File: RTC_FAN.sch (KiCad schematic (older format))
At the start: 9 parts

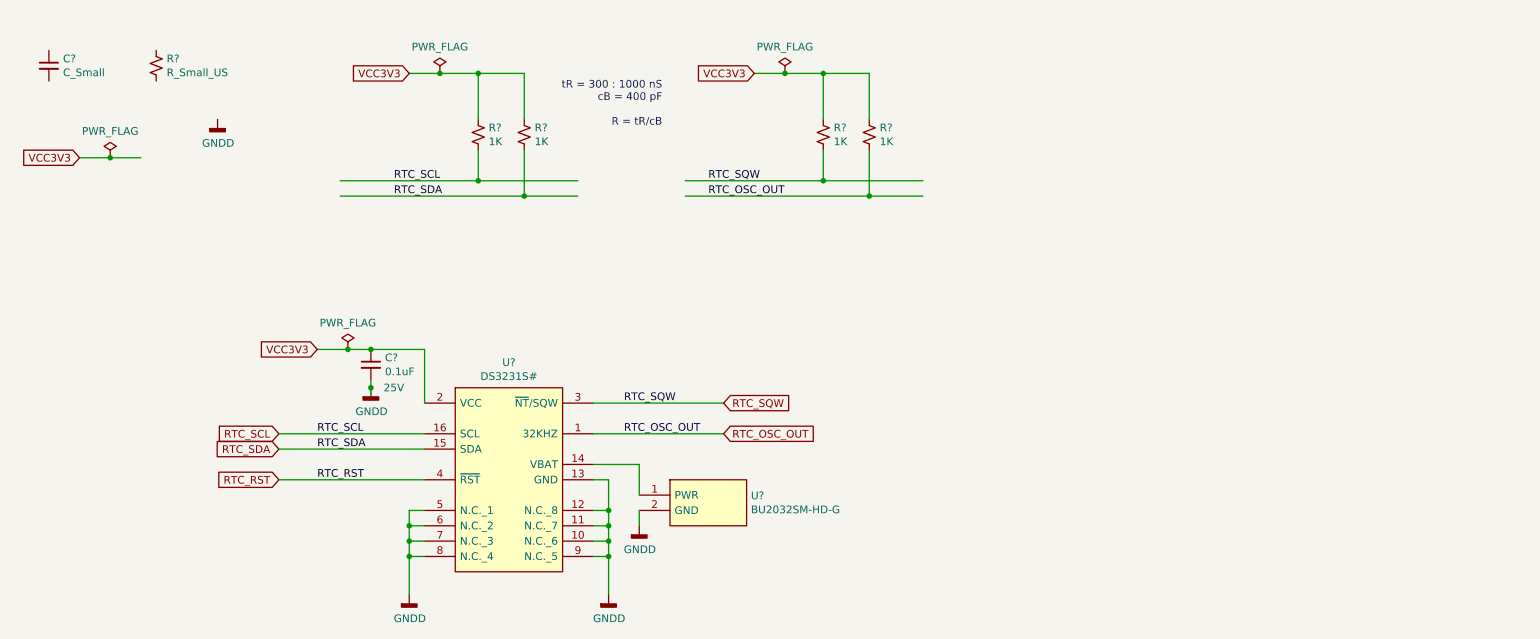
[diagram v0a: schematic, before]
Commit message: Added fan control circuitry
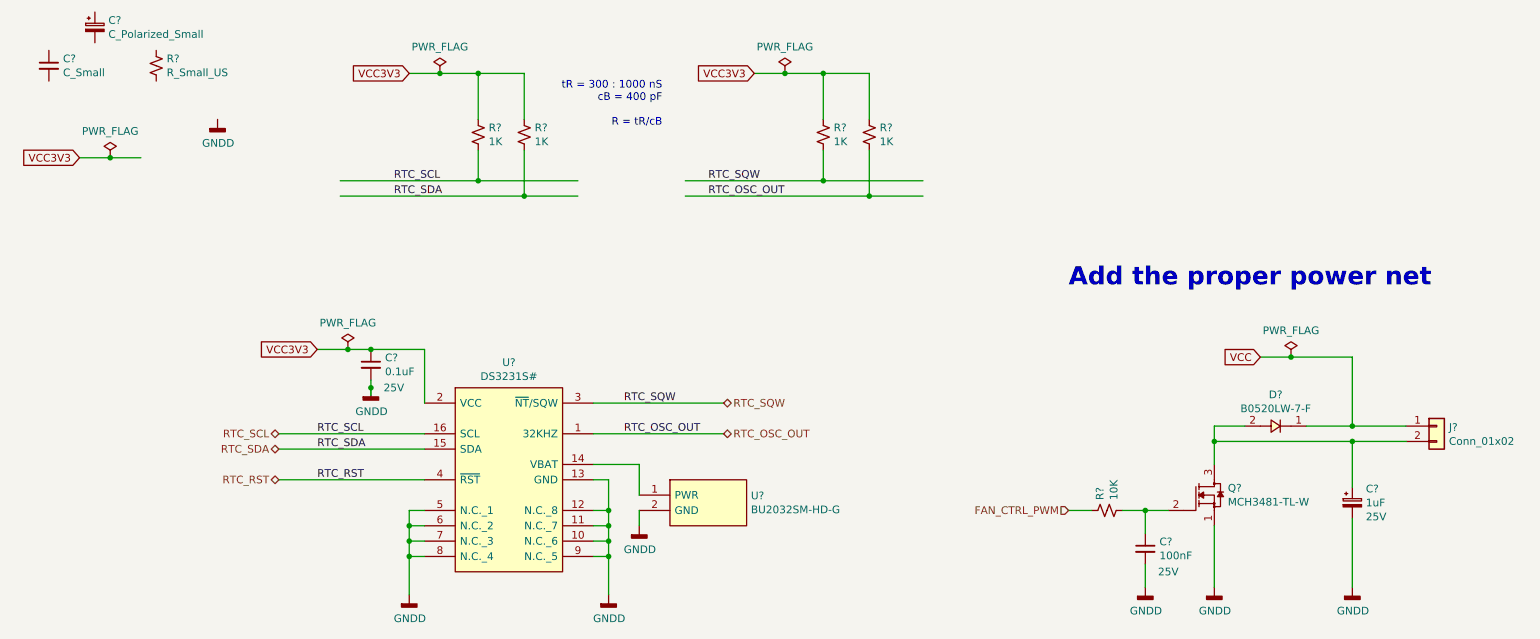
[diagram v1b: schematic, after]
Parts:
- added C?: 100nF, Capacitor_SMD:C_0603_1608Metric_Pad1.08x0.95mm_HandSolder, symbol Device:C_Small
- added C?: C_Polarized_Small, Capacitor_Tantalum_SMD:CP_EIA-1608-10_AVX-L_Pad1.25x1.05mm_HandSolder, symbol Device:C_Polarized_Small
- added C?: 1uF, Capacitor_Tantalum_SMD:CP_EIA-1608-10_AVX-L_Pad1.25x1.05mm_HandSolder, symbol Device:C_Polarized_Small
- added D?: B0520LW-7-F, SOD3716X145N, symbol GM_Diodes:B0520LW-7-F
- added J?: Conn_01x02, Connector_PinHeader_1.27mm:PinHeader_1x02_P1.27mm_Vertical, symbol Connector_Generic:Conn_01x02
- added Q?: MCH3481-TL-W, GM_SOT:SOT65P270X085-3N, symbol GM_MOSFET:MCH3481-TL-W
- added R?: 10K, Resistor_SMD:R_0603_1608Metric_Pad0.98x0.95mm_HandSolder, symbol Device:R_Small_US
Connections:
- net labels added: FAN_CTRL_PWM, VCC
- wire segments 56 -> 74
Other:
- note added: "Add the proper power net"
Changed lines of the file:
@@
 Text Label 4500 3300 0    50   ~ 0
-RTC_OSC_OUT
-Text GLabel 2250 3300 0    50   Input ~ 0
-RTC_SCL
-Text GLabel 2250 3400 0    50   Input ~ 0
-RTC_SDA
-Text GLabel 2250 3600 0    50   Input ~ 0
-RTC_RST
-Text GLabel 5150 3100 2    50   Input ~ 0
-RTC_SQW
-Text GLabel 5150 3300 2    50   Input ~ 0
 RTC_OSC_OUT
 Wire Wire Line
@@
 Wire Wire Line
 	4600 3500 4300 3500
+$Comp
+L GM_MOSFET:MCH3481-TL-W Q?
+U 1 1 602539F0
+P 8250 3700
+F 0 "Q?" H 8438 3746 50  0000 L CNN
+F 1 "MCH3481-TL-W" H 8438 3655 50  0000 L CNN
+F 2 "GM_SOT:SOT65P270X085-3N" H 9250 3900 50  0001 C CNN
+F 3 "https://www.onsemi.com/pub/Collateral/MCH3481-D.PDF" H 8250 4000 50  0001 C CNN
+F 4 "MCH3481-TL-W" H 9050 4000 50  0001 C CNN "MPN"
+	1    8250 3700
+	1    0    0    -1
+$EndComp
+$Comp
+L Device:R_Small_US R?
+U 1 1 60254F0F
+P 7650 3800
+AR Path="/601E7C5A/60254F0F" Ref="R?"  Part="1"
+AR Path="/601E7CC8/60254F0F" Ref="R?"  Part="1"
+F 0 "R?" H 7718 3846 50  0000 L CNN
+F 1 "10K" H 7718 3755 50  0000 L CNN
+F 2 "Resistor_SMD:R_0603_1608Metric_Pad0.98x0.95mm_HandSolder" H 7650 3800 50  0001 C CNN
+F 3 "~" H 7650 3800 50  0001 C CNN
+	1    7650 3800
+	0    -1   -1   0
+$EndComp
+$Comp
+L Device:C_Small C?
+U 1 1 60254F16
+P 7900 4050
+AR Path="/601E7C5A/60254F16" Ref="C?"  Part="1"
+AR Path="/601E7CC8/60254F16" Ref="C?"  Part="1"
+F 0 "C?" H 7992 4096 50  0000 L CNN
+F 1 "100nF" H 7992 4005 50  0000 L CNN
+F 2 "Capacitor_SMD:C_0603_1608Metric_Pad1.08x0.95mm_HandSolder" H 7900 4050 50  0001 C CNN
+F 3 "~" H 7900 4050 50  0001 C CNN
+F 4 "25V" H 8050 3900 50  0000 C CNN "Voltage"
+	1    7900 4050
+	1    0    0    -1
+$EndComp
+Wire Wire Line
+	7750 3800 7900 3800
+Wire Wire Line
+	7900 3950 7900 3800
+Connection ~ 7900 3800
+Wire Wire Line
+	7900 3800 8050 3800
+$Comp
+L power:GNDD #PWR?
+U 1 1 6025D5E9
+P 7900 4300
+AR Path="/601DF0A6/6025D5E9" Ref="#PWR?"  Part="1"
+AR Path="/601E7C5A/6025D5E9" Ref="#PWR?"  Part="1"
+AR Path="/601E7CC8/6025D5E9" Ref="#PWR?"  Part="1"
+F 0 "#PWR?" H 7900 4050 50  0001 C CNN
+F 1 "GNDD" H 7904 4145 50  0000 C CNN
+F 2 "" H 7900 4300 50  0001 C CNN
+F 3 "" H 7900 4300 50  0001 C CNN
+	1    7900 4300
+	1    0    0    -1
+$EndComp
+Text HLabel 2250 3300 0    50   BiDi ~ 0
+RTC_SCL
+Text HLabel 2250 3400 0    50   BiDi ~ 0
+RTC_SDA
+Text HLabel 2250 3600 0    50   BiDi ~ 0
+RTC_RST
+Text HLabel 5150 3300 2    50   BiDi ~ 0
+RTC_OSC_OUT
+Text HLabel 5150 3100 2    50   BiDi ~ 0
+RTC_SQW
+Text HLabel 7400 3800 0    50   Input ~ 0
+FAN_CTRL_PWM
+$Comp
+L power:GNDD #PWR?
+U 1 1 60263673
+P 8350 4300
+AR Path="/601DF0A6/60263673" Ref="#PWR?"  Part="1"
+AR Path="/601E7C5A/60263673" Ref="#PWR?"  Part="1"
+AR Path="/601E7CC8/60263673" Ref="#PWR?"  Part="1"
+F 0 "#PWR?" H 8350 4050 50  0001 C CNN
+F 1 "GNDD" H 8354 4145 50  0000 C CNN
+F 2 "" H 8350 4300 50  0001 C CNN
+F 3 "" H 8350 4300 50  0001 C CNN
+	1    8350 4300
+	1    0    0    -1
+$EndComp
+$Comp
+L Device:C_Polarized_Small C?
+U 1 1 60266E7E
+P 1050 650
+F 0 "C?" H 1138 696 50  0000 L CNN
+F 1 "C_Polarized_Small" H 1138 605 50  0000 L CNN
+F 2 "Capacitor_Tantalum_SMD:CP_EIA-1608-10_AVX-L_Pad1.25x1.05mm_HandSolder" H 1050 650 50  0001 C CNN
+F 3 "~" H 1050 650 50  0001 C CNN
+F 4 "" H 1050 650 50  0000 C CNN "Voltage"
+	1    1050 650
+	1    0    0    -1
+$EndComp
+$Comp
+L Device:C_Polarized_Small C?
+U 1 1 60269FC6
+P 9250 3750
+F 0 "C?" H 9338 3841 50  0000 L CNN
+F 1 "1uF" H 9338 3750 50  0000 L CNN
+F 2 "Capacitor_Tantalum_SMD:CP_EIA-1608-10_AVX-L_Pad1.25x1.05mm_HandSolder" H 9250 3750 50  0001 C CNN
+F 3 "~" H 9250 3750 50  0001 C CNN
+F 4 "25V" H 9338 3659 50  0000 L CNN "Voltage"
+	1    9250 3750
+	1    0    0    -1
+$EndComp
+$Comp
+L Connector_Generic:Conn_01x02 J?
+U 1 1 60278B21
+P 9800 3250
+F 0 "J?" H 9880 3242 50  0000 L CNN
+F 1 "Conn_01x02" H 9880 3151 50  0000 L CNN
+F 2 "Connector_PinHeader_1.27mm:PinHeader_1x02_P1.27mm_Vertical" H 9800 3250 50  0001 C CNN
+F 3 "~" H 9800 3250 50  0001 C CNN
+	1    9800 3250
+	1    0    0    -1
+$EndComp
+Wire Wire Line
+	8350 3500 8350 3350
+Wire Wire Line
+	8350 3350 9250 3350
+Wire Wire Line
+	9250 3650 9250 3350
+Connection ~ 9250 3350
+Wire Wire Line
+	9250 3350 9600 3350
+$Comp
+L power:GNDD #PWR?
+U 1 1 6028129F
+P 9250 4300
+AR Path="/601DF0A6/6028129F" Ref="#PWR?"  Part="1"
+AR Path="/601E7C5A/6028129F" Ref="#PWR?"  Part="1"
+AR Path="/601E7CC8/6028129F" Ref="#PWR?"  Part="1"
+F 0 "#PWR?" H 9250 4050 50  0001 C CNN
+F 1 "GNDD" H 9254 4145 50  0000 C CNN
+F 2 "" H 9250 4300 50  0001 C CNN
+F 3 "" H 9250 4300 50  0001 C CNN
+	1    9250 4300
+	1    0    0    -1
+$EndComp
+Wire Wire Line
+	9250 4300 9250 3850
+Wire Wire Line
+	8350 4300 8350 3900
+Wire Wire Line
+	7900 4300 7900 4150
+Wire Wire Line
+	7550 3800 7400 3800
+$Comp
+L GM_Diodes:B0520LW-7-F D?
+U 1 1 6029EC80
+P 8750 3250
+F 0 "D?" H 8750 3045 50  0000 C CNN
+F 1 "B0520LW-7-F" H 8750 3136 50  0000 C CNN
+F 2 "SOD3716X145N" H 9250 3250 50  0001 L CNN
+F 3 "https://www.diodes.com/assets/Datasheets/ds30051.pdf" H 9200 3150 50  0001 L CNN
+F 4 "B0520LW-7-F" H 9450 3150 50  0001 C CNN "MPN"
+	1    8750 3250
+	-1   0    0    1
+$EndComp
+Wire Wire Line
+	8950 3250 9250 3250
+Wire Wire Line
+	8550 3250 8350 3250
+Wire Wire Line
+	8350 3250 8350 3350
+Connection ~ 8350 3350
+Text GLabel 8650 2800 0    50   Input ~ 0
+VCC
+$Comp
+L power:PWR_FLAG #FLG?
+U 1 1 602A4D12
+P 8850 2800
+AR Path="/601E7C5A/602A4D12" Ref="#FLG?"  Part="1"
+AR Path="/601E7CC8/602A4D12" Ref="#FLG?"  Part="1"
+F 0 "#FLG?" H 8850 2875 50  0001 C CNN
+F 1 "PWR_FLAG" H 8850 2973 50  0000 C CNN
+F 2 "" H 8850 2800 50  0001 C CNN
+F 3 "~" H 8850 2800 50  0001 C CNN
+	1    8850 2800
+	1    0    0    -1
+$EndComp
+Connection ~ 8850 2800
+Wire Wire Line
+	8650 2800 8850 2800
+Wire Wire Line
+	9250 2800 9250 3250
+Wire Wire Line
+	8850 2800 9250 2800
+Connection ~ 9250 3250
+Wire Wire Line
+	9250 3250 9600 3250
+Text Notes 7400 2350 0    118  ~ 24
+Add the proper power net
 $EndSCHEMATC

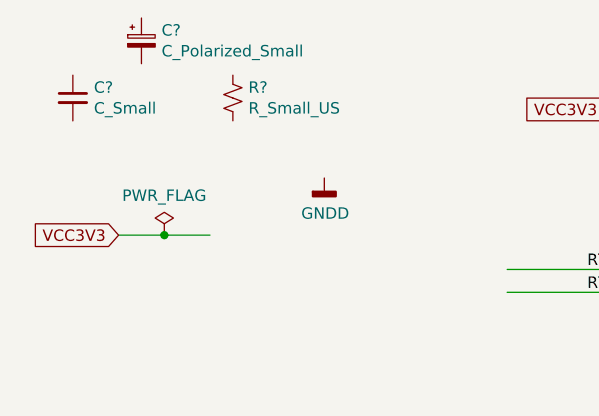
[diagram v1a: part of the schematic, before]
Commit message: Added new sheet for Ethernet PHY Connector and drawn schematic (continue)
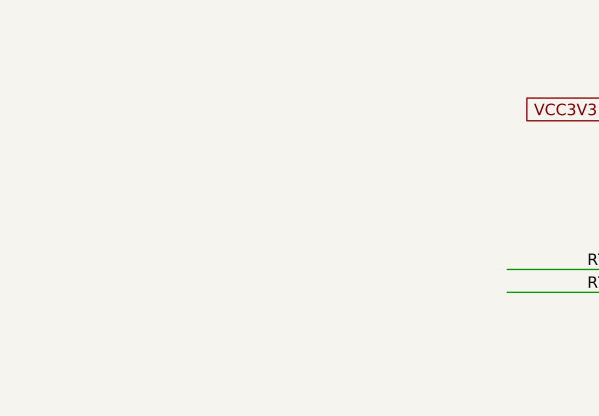
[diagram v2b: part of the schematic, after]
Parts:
- removed C?: C_Small, Capacitor_SMD:C_0603_1608Metric_Pad1.08x0.95mm_HandSolder, symbol Device:C_Small
- removed C?: C_Polarized_Small, Capacitor_Tantalum_SMD:CP_EIA-1608-10_AVX-L_Pad1.25x1.05mm_HandSolder, symbol Device:C_Polarized_Small
- removed R?: R_Small_US, Resistor_SMD:R_0603_1608Metric_Pad0.98x0.95mm_HandSolder, symbol Device:R_Small_US
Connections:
- wire segments 74 -> 72
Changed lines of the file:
@@
 $Descr A4 11693 8268
 encoding utf-8
-Sheet 12 14
+Sheet 12 15
 Title "CGMPCX1006"
 Date "2021-02-03"
@@
 F 4 "DS3231S#" H 3400 3000 50  0001 C CNN "MPN"
 	1    3400 3000
-	1    0    0    -1
-$EndComp
-$Comp
-L Device:R_Small_US R?
-U 1 1 6022D309
-P 1450 900
-AR Path="/601E7C5A/6022D309" Ref="R?"  Part="1"
-AR Path="/601E7CC8/6022D309" Ref="R?"  Part="1"
-F 0 "R?" H 1518 946 50  0000 L CNN
-F 1 "R_Small_US" H 1518 855 50  0000 L CNN
-F 2 "Resistor_SMD:R_0603_1608Metric_Pad0.98x0.95mm_HandSolder" H 1450 900 50  0001 C CNN
-F 3 "~" H 1450 900 50  0001 C CNN
-	1    1450 900
-	1    0    0    -1
-$EndComp
-$Comp
-L Device:C_Small C?
-U 1 1 6022D310
-P 750 900
-AR Path="/601E7C5A/6022D310" Ref="C?"  Part="1"
-AR Path="/601E7CC8/6022D310" Ref="C?"  Part="1"
-F 0 "C?" H 842 946 50  0000 L CNN
-F 1 "C_Small" H 842 855 50  0000 L CNN
-F 2 "Capacitor_SMD:C_0603_1608Metric_Pad1.08x0.95mm_HandSolder" H 750 900 50  0001 C CNN
-F 3 "~" H 750 900 50  0001 C CNN
-F 4 "" H 750 900 50  0000 C CNN "Voltage"
-	1    750  900
-	1    0    0    -1
-$EndComp
-Text GLabel 950  1500 0    50   Input ~ 0
-VCC3V3
-$Comp
-L power:PWR_FLAG #FLG?
-U 1 1 6022D9C5
-P 1150 1500
-AR Path="/601E7C5A/6022D9C5" Ref="#FLG?"  Part="1"
-AR Path="/601E7CC8/6022D9C5" Ref="#FLG?"  Part="1"
-F 0 "#FLG?" H 1150 1575 50  0001 C CNN
-F 1 "PWR_FLAG" H 1150 1673 50  0000 C CNN
-F 2 "" H 1150 1500 50  0001 C CNN
-F 3 "~" H 1150 1500 50  0001 C CNN
-	1    1150 1500
-	1    0    0    -1
-$EndComp
-Connection ~ 1150 1500
-Wire Wire Line
-	1150 1500 1350 1500
-Wire Wire Line
-	950  1500 1150 1500
-$Comp
-L power:GNDD #PWR?
-U 1 1 6022DF01
-P 1850 1250
-AR Path="/601DF0A6/6022DF01" Ref="#PWR?"  Part="1"
-AR Path="/601E7C5A/6022DF01" Ref="#PWR?"  Part="1"
-AR Path="/601E7CC8/6022DF01" Ref="#PWR?"  Part="1"
-F 0 "#PWR?" H 1850 1000 50  0001 C CNN
-F 1 "GNDD" H 1854 1095 50  0000 C CNN
-F 2 "" H 1850 1250 50  0001 C CNN
-F 3 "" H 1850 1250 50  0001 C CNN
-	1    1850 1250
 	1    0    0    -1
 $EndComp
@@
 	1    0    0    -1
 $EndComp
-$Comp
-L Device:C_Polarized_Small C?
-U 1 1 60266E7E
-P 1050 650
-F 0 "C?" H 1138 696 50  0000 L CNN
-F 1 "C_Polarized_Small" H 1138 605 50  0000 L CNN
-F 2 "Capacitor_Tantalum_SMD:CP_EIA-1608-10_AVX-L_Pad1.25x1.05mm_HandSolder" H 1050 650 50  0001 C CNN
-F 3 "~" H 1050 650 50  0001 C CNN
-F 4 "" H 1050 650 50  0000 C CNN "Voltage"
-	1    1050 650
-	1    0    0    -1
-$EndComp
